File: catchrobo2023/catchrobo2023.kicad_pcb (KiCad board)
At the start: 2 copper layers, 72 x 47 mm, 38 parts, among them J1 Conn_01x03_Male, J2 Conn_01x03_Male, J3 Conn_01x03_Male, J4 Conn_01x02_Male, J5 Conn_01x02_Male, J6 Conn_01x02_Male, J7 Conn_01x02_Male, J8 Conn_01x02_Male, Q1 AO3401A, SW1 SW_SPDT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

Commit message: 製造ファイルまで出力
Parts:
- moved J4 1.34 mm to (102.5, 81.0)
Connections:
- U8 pad 13: /Sensor2 -> /Sensor0
- U8 pad 15: /Sensor0 -> /Sensor2
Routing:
- net /Sensor2: track 12.2 -> 15.6 mm, vias 0 -> 1
- net /Sensor0: track 16.3 -> 15.1 mm, vias 0 -> 1
- net /Stopper: track 29.0 -> 29.6 mm
- net GND: track 0.04 -> 0.00 mm, vias 169 -> 172
- net (no net): vias 0 -> 1
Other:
- board text added: "5V"
- board text added: "GND"
- board text added: "Signal"

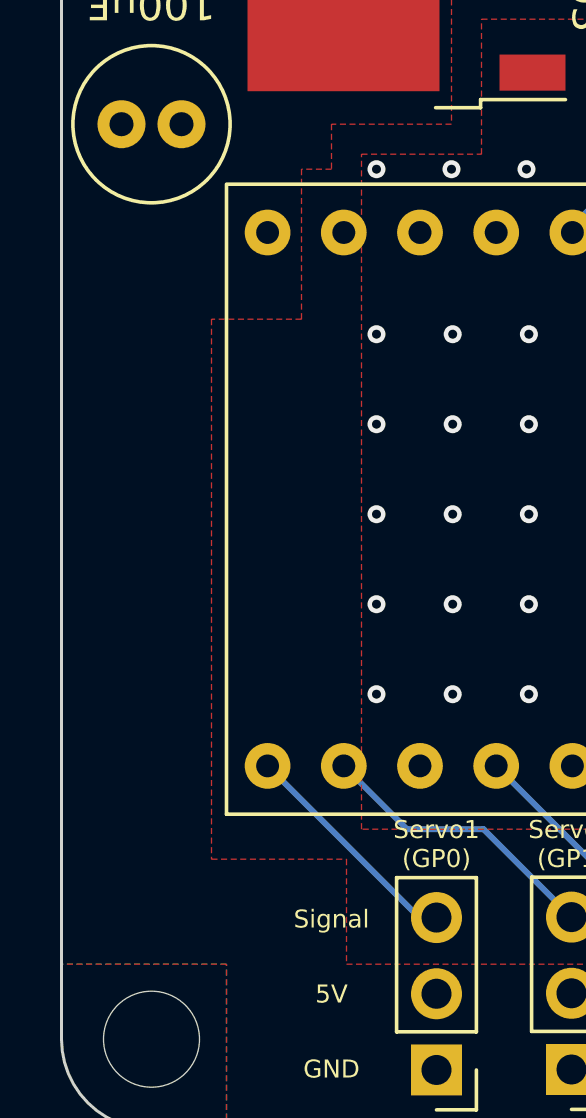
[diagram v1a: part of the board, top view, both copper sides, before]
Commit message: ロゴの追加
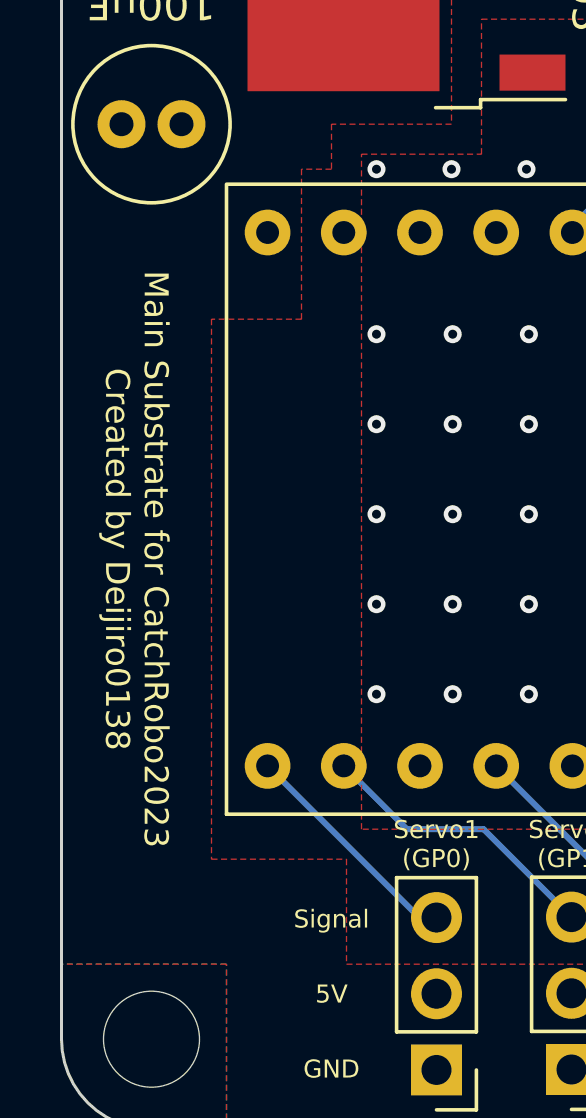
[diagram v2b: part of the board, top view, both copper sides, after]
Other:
- board text added: "Main Substrate for CatchRobo2023 Created by Deijiro0138"
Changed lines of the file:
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@@
     (effects (font (size 0.6 0.6) (thickness 0.15)))
+  )
+  (gr_text "Main Substrate for CatchRobo2023\nCreated by Deijiro0138" (at 82.5 101 270) (layer "F.SilkS")
+    (effects (font (size 0.8 0.8) (thickness 0.15)))
   )
   (gr_text "Mode Switch" (at 143.5 77 180) (layer "F.SilkS")
